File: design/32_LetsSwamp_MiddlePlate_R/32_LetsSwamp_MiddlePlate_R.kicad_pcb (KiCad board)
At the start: 2 copper layers, 122.6 x 85.3 mm, 0 parts

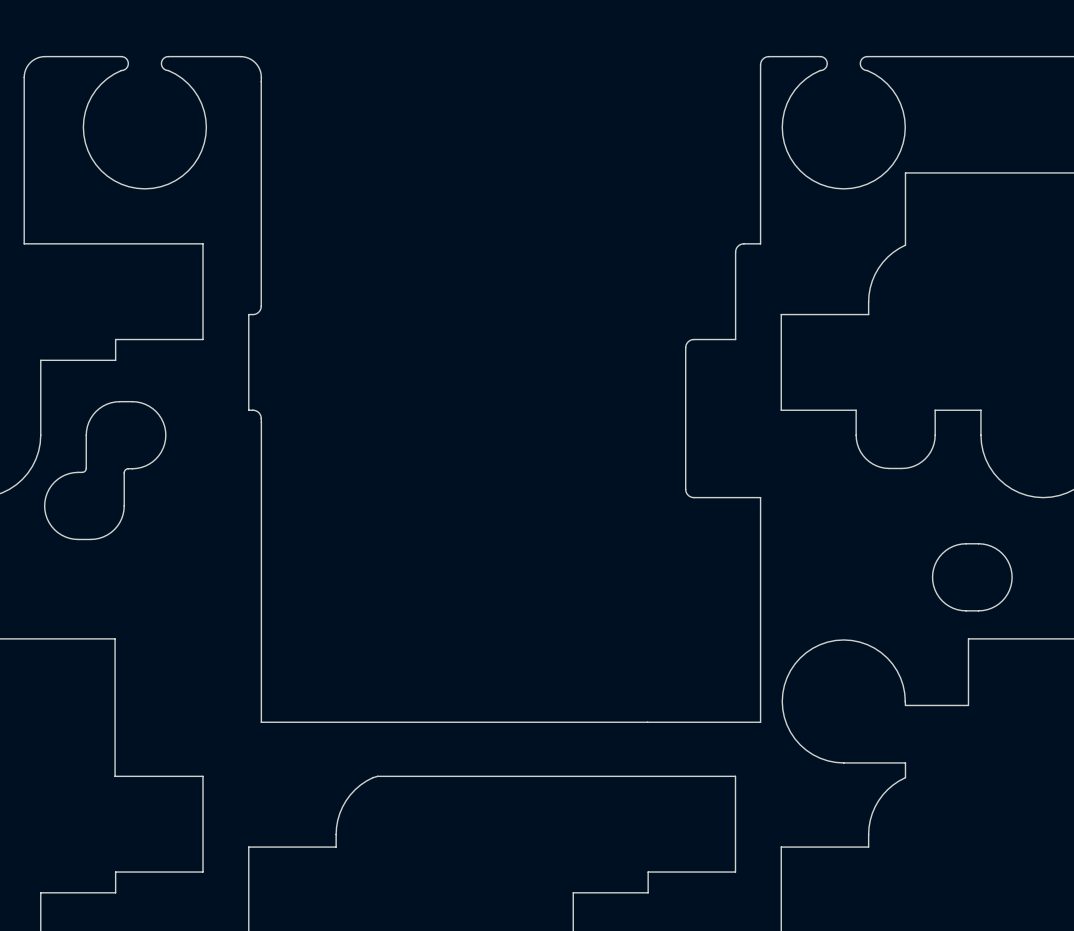
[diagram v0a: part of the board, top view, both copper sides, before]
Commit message: Modify middle plates
avoid to pin sockets and some diodes
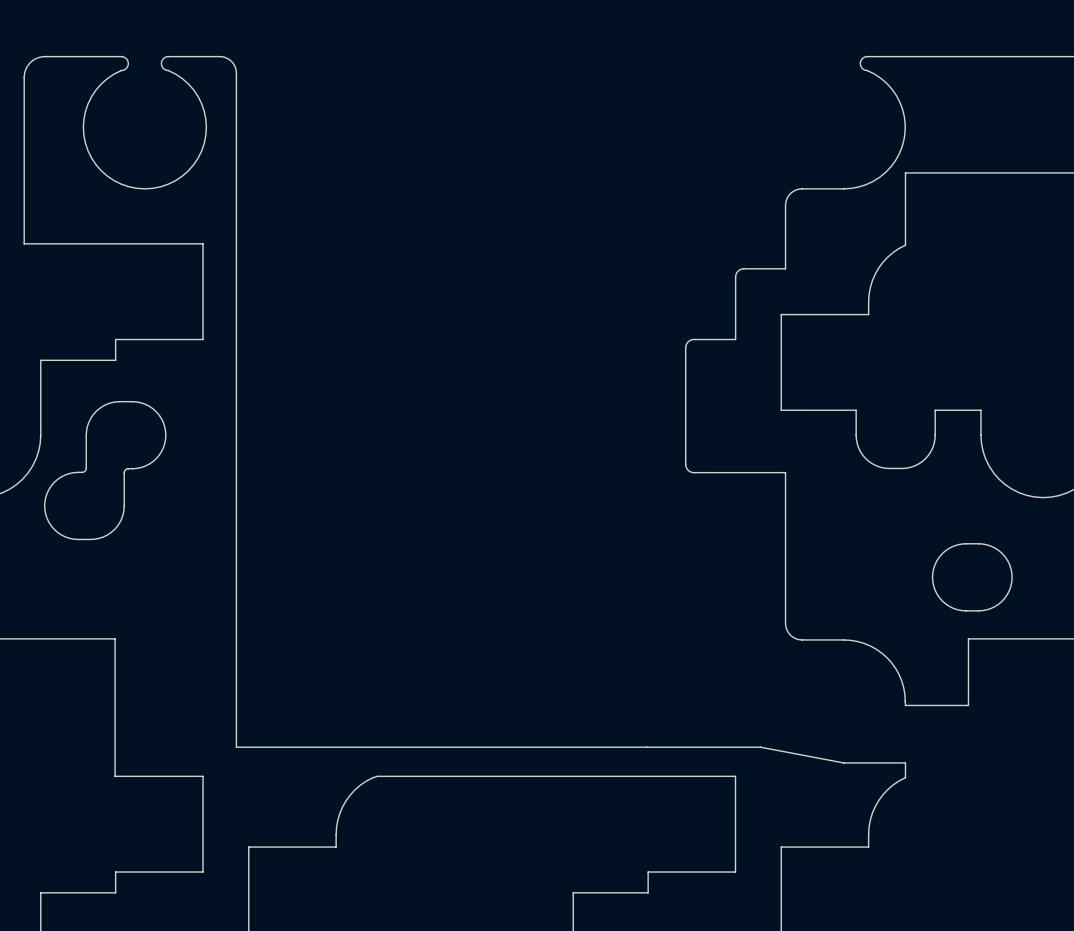
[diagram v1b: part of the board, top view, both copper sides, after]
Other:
- outline, holes or cut-outs redrawn
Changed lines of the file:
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@@
   (general
     (thickness 1.6)
-    (drawings 885)
+    (drawings 879)
     (tracks 0)
     (zones 0)
@@
     (uvia_drill 0.1)
   )
+  (gr_arc (start 29.472025 6.729701) (end 28.876713 6.729701) (angle -90) (layer Edge.Cuts) (width 0.05))
+  (gr_arc (start 29.472026 -8.217983) (end 29.472026 -8.813295) (angle -90) (layer Edge.Cuts) (width 0.05))
+  (gr_line (start 29.472026 7.325013) (end 30.956004 7.325013) (layer Edge.Cuts) (width 0.05))
+  (gr_line (start 27.983744 11.162101) (end 30.960164 11.725007) (layer Edge.Cuts) (width 0.05))
+  (gr_arc (start 8.636103 -12.949208) (end 9.231415 -12.949208) (angle -90) (layer Edge.Cuts) (width 0.05))
+  (gr_line (start 29.472026 -8.813295) (end 30.956004 -8.813295) (layer Edge.Cuts) (width 0.05))
   (gr_line (start 100.468245 59.680076) (end 100.468245 58.498717) (layer Edge.Cuts) (width 0.05))
   (gr_arc (start 98.961435 58.331359) (end 98.961435 58.480187) (angle -90) (layer Edge.Cuts) (width 0.05))
@@
   )
   (gr_line (start 104.797756 71.73634) (end -9.543756 71.73634) (layer Edge.Cuts) (width 0.05))
-  (gr_arc (start 25.602496 1.934764) (end 25.30484 1.934764) (angle -90) (layer Edge.Cuts) (width 0.05))
-  (gr_arc (start 28.2814 -13.245692) (end 27.983744 -13.245692) (angle 90) (layer Edge.Cuts) (width 0.05))
-  (gr_line (start 10.124384 -0.446484) (end 10.124384 10.269132) (layer Edge.Cuts) (width 0.05))
-  (gr_arc (start 27.388432 -6.548432) (end 27.388432 -6.846088) (angle -90) (layer Edge.Cuts) (width 0.05))
+  (gr_arc (start 25.602496 1.041795) (end 25.30484 1.041795) (angle -90) (layer Edge.Cuts) (width 0.05))
+  (gr_line (start 9.231415 -12.949208) (end 9.231415 11.162101) (layer Edge.Cuts) (width 0.05))
+  (gr_arc (start 27.388496 -5.655463) (end 27.388496 -5.953119) (angle -90) (layer Edge.Cuts) (width 0.05))
   (gr_arc (start 25.602496 -3.125388) (end 25.602496 -3.423044) (angle -90) (layer Edge.Cuts) (width 0.05))
-  (gr_line (start 27.983744 10.269132) (end 27.983744 2.232422) (layer Edge.Cuts) (width 0.05))
-  (gr_line (start 25.30484 1.934764) (end 25.30484 -3.125388) (layer Edge.Cuts) (width 0.05))
-  (gr_line (start 23.940228 10.269132) (end 27.983744 10.269132) (layer Edge.Cuts) (width 0.05))
+  (gr_line (start 28.876713 6.729701) (end 28.876713 1.339451) (layer Edge.Cuts) (width 0.05))
+  (gr_line (start 25.30484 1.041795) (end 25.30484 -3.125388) (layer Edge.Cuts) (width 0.05))
+  (gr_line (start 23.940228 11.162101) (end 27.983744 11.162101) (layer Edge.Cuts) (width 0.05))
   (gr_circle (center 11.433936 3.740545) (end 10.162349 3.740545) (layer Dwgs.User) (width 0.05))
   (gr_circle (center 11.433936 8.820545) (end 10.162349 8.820545) (layer Dwgs.User) (width 0.05))
-  (gr_arc (start 30.960164 9.525008) (end 33.160163 9.525008) (angle -270) (layer Edge.Cuts) (width 0.05))
+  (gr_arc (start 30.960164 9.525008) (end 33.160163 9.525008) (angle -90.10834337) (layer Edge.Cuts) (width 0.05))
   (gr_circle (center 11.433936 6.280545) (end 10.162349 6.280545) (layer Dwgs.User) (width 0.05))
-  (gr_line (start 25.602496 2.23242) (end 27.983744 2.232422) (layer Edge.Cuts) (width 0.05))
+  (gr_line (start 25.602496 1.339451) (end 28.876713 1.339451) (layer Edge.Cuts) (width 0.05))
   (gr_line (start 43.011324 15.626956) (end 46.136712 15.626956) (layer Edge.Cuts) (width 0.05))
   (gr_line (start 31.849224 14.287504) (end 31.849224 14.733988) (layer Edge.Cuts) (width 0.05))
@@
   (gr_line (start 46.136712 12.203912) (end 45.669134 12.203912) (layer Edge.Cuts) (width 0.05))
   (gr_line (start 40.33242 19.05) (end 40.33242 16.371096) (layer Edge.Cuts) (width 0.05))
-  (gr_line (start 27.09084 -3.423044) (end 27.090776 -6.548432) (layer Edge.Cuts) (width 0.05))
-  (gr_line (start 27.983744 -6.846088) (end 27.388432 -6.846088) (layer Edge.Cuts) (width 0.05))
-  (gr_line (start 27.983744 -6.846088) (end 27.983744 -13.245692) (layer Edge.Cuts) (width 0.05))
-  (gr_arc (start 9.379072 -12.799208) (end 10.124384 -12.799208) (angle -90) (layer Edge.Cuts) (width 0.05))
+  (gr_line (start 27.09084 -3.423044) (end 27.09084 -5.655463) (layer Edge.Cuts) (width 0.05))
+  (gr_line (start 28.876713 -5.953119) (end 27.388496 -5.953119) (layer Edge.Cuts) (width 0.05))
+  (gr_line (start 28.876713 -5.953119) (end 28.876713 -8.217983) (layer Edge.Cuts) (width 0.05))
   (gr_arc (start 31.802069 -13.295173) (end 31.802069 -13.045826) (angle 179.9997702) (layer Edge.Cuts) (width 0.05))
-  (gr_arc (start 30.11826 -13.295173) (end 30.11826 -13.54452) (angle 179.9997702) (layer Edge.Cuts) (width 0.05))
   (gr_line (start 25.602496 -3.423044) (end 27.09084 -3.423044) (layer Edge.Cuts) (width 0.05))
-  (gr_line (start 30.11826 -13.54452) (end 28.2814 -13.543348) (layer Edge.Cuts) (width 0.05))
-  (gr_arc (start 30.960164 -11.013291) (end 31.802068 -13.045826) (angle 315) (layer Edge.Cuts) (width 0.05))
+  (gr_arc (start 30.960164 -11.013291) (end 31.802068 -13.045826) (angle 157.6083327) (layer Edge.Cuts) (width 0.05))
   (gr_line (start 2.23242 0) (end 2.23242 -2.678904) (layer Edge.Cuts) (width 0.05))
   (gr_line (start 2.23242 19.05) (end 2.23242 16.371096) (layer Edge.Cuts) (width 0.05))
@@
   (gr_arc (start 15.031644 14.287504) (end 12.799224 14.287504) (angle 65.83806624) (layer Edge.Cuts) (width 0.05))
   (gr_line (start 23.961324 15.626956) (end 27.086712 15.626956) (layer Edge.Cuts) (width 0.05))
-  (gr_line (start 10.120304 10.269132) (end 23.940228 10.269132) (layer Edge.Cuts) (width 0.05))
+  (gr_line (start 9.231415 11.162101) (end 23.940228 11.162101) (layer Edge.Cuts) (width 0.05))
   (gr_line (start 33.16758 9.667968) (end 33.160163 9.525008) (layer Edge.Cuts) (width 0.05))
   (gr_line (start 78.43242 -2.678904) (end 81.111324 -2.678904) (layer Edge.Cuts) (width 0.05))
   (gr_line (start 69.949224 -4.762496) (end 69.949224 -4.316012) (layer Edge.Cuts) (width 0.05))
-  (gr_line (start 9.822648 -4.316012) (end 9.673884 -4.316012) (layer Edge.Cuts) (width 0.05))
   (gr_line (start 97.48242 -2.678904) (end 100.161324 -2.678904) (layer Edge.Cuts) (width 0.05))
-  (gr_line (start 10.124384 -0.446484) (end 10.120304 -0.595312) (layer Edge.Cuts) (width 0.05))
-  (gr_arc (start 9.822648 -4.613668) (end 9.822648 -4.316012) (angle -90) (layer Edge.Cuts) (width 0.05))
-  (gr_line (start 10.120304 -12.65038) (end 10.124384 -12.799208) (layer Edge.Cuts) (width 0.05))
   (gr_line (start 88.999224 -4.762496) (end 88.999224 -4.316012) (layer Edge.Cuts) (width 0.05))
   (gr_line (start 103.286712 -3.423044) (end 103.286712 -6.846088) (layer Edge.Cuts) (width 0.05))
@@
   (gr_line (start 90.31758 -9.382032) (end 90.31758 -6.8) (layer Edge.Cuts) (width 0.05))
   (gr_line (start 100.161324 -2.678904) (end 100.161324 -3.423044) (layer Edge.Cuts) (width 0.05))
-  (gr_line (start 9.673884 -0.892968) (end 9.822648 -0.892968) (layer Edge.Cuts) (width 0.05))
-  (gr_line (start 9.673884 -4.316012) (end 9.673884 -0.892968) (layer Edge.Cuts) (width 0.05))
   (gr_line (start 97.48242 0) (end 97.48242 -2.678904) (layer Edge.Cuts) (width 0.05))
-  (gr_arc (start 9.822648 -0.595312) (end 10.120304 -0.595312) (angle -90) (layer Edge.Cuts) (width 0.05))
   (gr_line (start 100.140228 -6.846088) (end 100.140228 -9.382032) (layer Edge.Cuts) (width 0.05))
   (gr_line (start 103.286712 -6.846088) (end 100.140228 -6.846088) (layer Edge.Cuts) (width 0.05))
@@
   (gr_arc (start -12.929696 -5.95312) (end -13.675008 -5.95312) (angle 90) (layer Edge.Cuts) (width 0.05))
   (gr_line (start 1.640016 -6.846088) (end 1.640016 -12.799208) (layer Edge.Cuts) (width 0.05))
-  (gr_line (start 9.379072 -13.54452) (end 6.798954 -13.54452) (layer Edge.Cuts) (width 0.05))
+  (gr_line (start 8.636103 -13.54452) (end 6.798954 -13.54452) (layer Edge.Cuts) (width 0.05))
   (gr_line (start 108.929008 8.683104) (end 108.929008 -9.413291) (layer Edge.Cuts) (width 0.05))
   (gr_line (start -12.929696 -6.698432) (end -5.20898 -6.69726) (layer Edge.Cuts) (width 0.05))
@@
   (gr_arc (start 2.385328 -12.799208) (end 2.385328 -13.54452) (angle -90) (layer Edge.Cuts) (width 0.05))
   (gr_line (start 103.862035 -13.54452) (end 31.802068 -13.54452) (layer Edge.Cuts) (width 0.05))
-  (gr_line (start 10.120304 -4.613668) (end 10.120304 -12.65038) (layer Edge.Cuts) (width 0.05))
   (gr_line (start -6.250776 -4.316012) (end -9.376164 -4.316012) (layer Edge.Cuts) (width 0.05))
   (gr_arc (start -11.143756 9.525008) (end -13.176291 8.683104) (angle 315) (layer Edge.Cuts) (width 0.05))
